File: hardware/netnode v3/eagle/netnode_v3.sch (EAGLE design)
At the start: 29 parts, among them IC1 TSR-1, IC2 PIC18F4K80, IC3 FOD060L, X1 DC10R, X2 XPORT

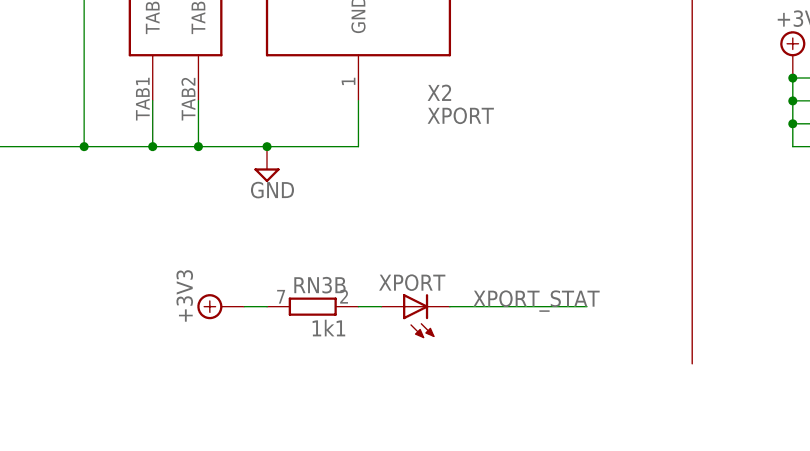
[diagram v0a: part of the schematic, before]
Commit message: Further board cleanup
* Silkscreen fixes + size increased
* Replaced 0603 componentsn with 0805 counterparts for easier soldering
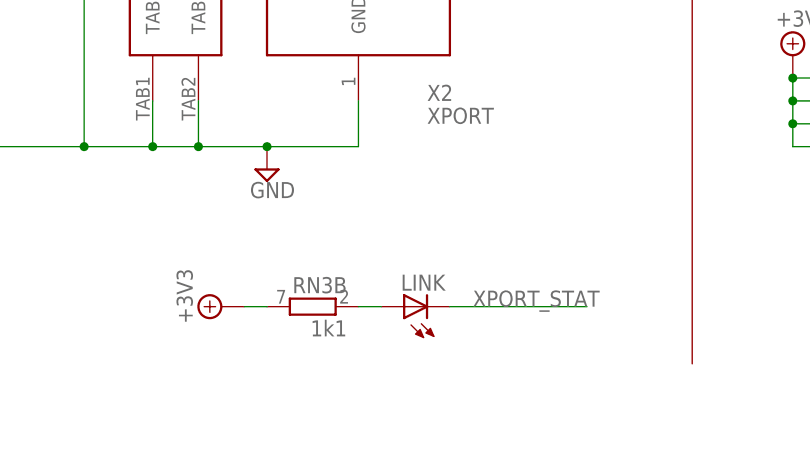
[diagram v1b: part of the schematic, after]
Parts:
- C1, C7: device netnode:C-EUC0603 -> rcl:C-EUC0805
- C3, C4: device rcl:C-EUC0603 -> rcl:C-EUC0805
- R1, R7: device rcl:R-EU_R0603 -> rcl:R-EU_R0805
- renumbered XPORT to LINK
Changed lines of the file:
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@@
 <attribute name="OC_FARNELL" value="8530025"/>
 </part>
-<part name="XPORT" library="led" deviceset="LED" device="CHIPLED_1206">
+<part name="LINK" library="led" deviceset="LED" device="CHIPLED_1206">
 <attribute name="MF" value="KINGBRIGHT"/>
 <attribute name="MPN" value="KP-3216EC"/>
@@
 <part name="V3" library="netnode" deviceset="+3V3" device=""/>
 <part name="V4" library="netnode" deviceset="+3V3" device=""/>
-<part name="C1" library="netnode" deviceset="C-EU" device="C0603" value="100n">
+<part name="C1" library="rcl" deviceset="C-EU" device="C0805" value="100n">
 <attribute name="MF" value="AVX"/>
 <attribute name="MPN" value="08055C104JAT2A"/>
@@
 <attribute name="OC_FARNELL" value="1823169"/>
 </part>
-<part name="R7" library="rcl" deviceset="R-EU_" device="R0603" value="2K">
+<part name="R7" library="rcl" deviceset="R-EU_" device="R0805" value="2K">
 <attribute name="MF" value="BOURNS"/>
 <attribute name="MPN" value="CR0603-FX-2001ELF"/>
@@
 </part>
 <part name="V11" library="netnode" deviceset="+3V3" device=""/>
-<part name="C3" library="rcl" deviceset="C-EU" device="C0603" value="100n">
+<part name="C3" library="rcl" deviceset="C-EU" device="C0805" value="100n">
 <attribute name="MF" value="AVX"/>
 <attribute name="MPN" value="08055C104JAT2A"/>
 <attribute name="OC_FARNELL" value="1740673"/>
 </part>
-<part name="C4" library="rcl" deviceset="C-EU" device="C0603" value="100n">
+<part name="C4" library="rcl" deviceset="C-EU" device="C0805" value="100n">
 <attribute name="MF" value="AVX"/>
 <attribute name="MPN" value="08055C104JAT2A"/>
@@
 </part>
 <part name="V26" library="supply2" deviceset="GND" device=""/>
-<part name="C7" library="netnode" deviceset="C-EU" device="C0603" value="100n">
+<part name="C7" library="rcl" deviceset="C-EU" device="C0805" value="100n">
 <attribute name="MF" value="AVX"/>
 <attribute name="MPN" value="08055C104JAT2A"/>
@@
 <part name="V34" library="netnode" deviceset="+3V3" device=""/>
 <part name="V35" library="netnode" deviceset="+3V3" device=""/>
-<part name="R1" library="rcl" deviceset="R-EU_" device="R0603" value="2K">
+<part name="R1" library="rcl" deviceset="R-EU_" device="R0805" value="2K">
 <attribute name="MF" value="BOURNS"/>
 <attribute name="MPN" value="CR0603-FX-2001ELF"/>
@@
 <attribute name="MPN" x="55.88" y="101.6" size="1.778" layer="96" rot="R90" display="off"/>
 </instance>
-<instance part="XPORT" gate="G$1" x="55.88" y="10.16" rot="R90">
+<instance part="LINK" gate="G$1" x="55.88" y="10.16" rot="R90">
 <attribute name="OC_FARNELL" x="55.88" y="10.16" size="1.778" layer="96" rot="R90" display="off"/>
 <attribute name="MF" x="55.88" y="10.16" size="1.778" layer="96" rot="R90" display="off"/>
@@
 </segment>
 <segment>
-<pinref part="XPORT" gate="G$1" pin="C"/>
+<pinref part="LINK" gate="G$1" pin="C"/>
 <wire x1="60.96" y1="10.16" x2="76.2" y2="10.16" width="0.1524" layer="91"/>
 <label x="63.5" y="10.16" size="1.778" layer="95"/>
@@
 <net name="N$1" class="1">
 <segment>
-<pinref part="XPORT" gate="G$1" pin="A"/>
+<pinref part="LINK" gate="G$1" pin="A"/>
 <wire x1="50.8" y1="10.16" x2="53.34" y2="10.16" width="0.1524" layer="91"/>
 <pinref part="RN3" gate="B" pin="1"/>

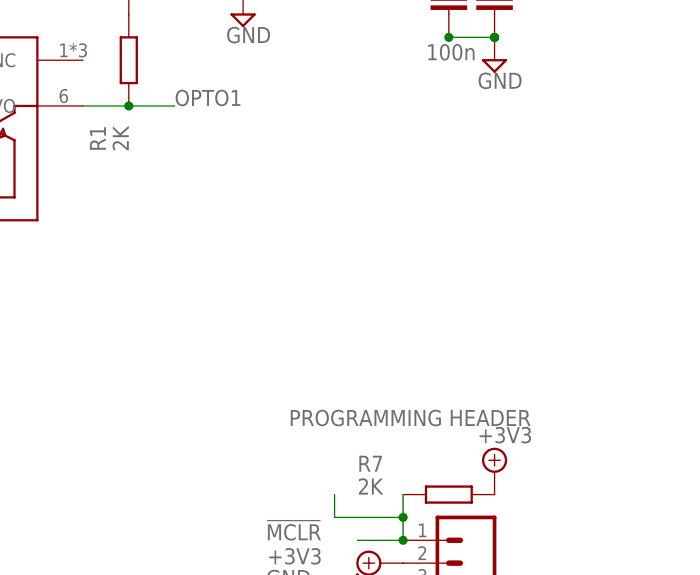
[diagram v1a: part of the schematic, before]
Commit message: Added reset button.
The reset button from Wuerth is a handy addition when developing firmware.
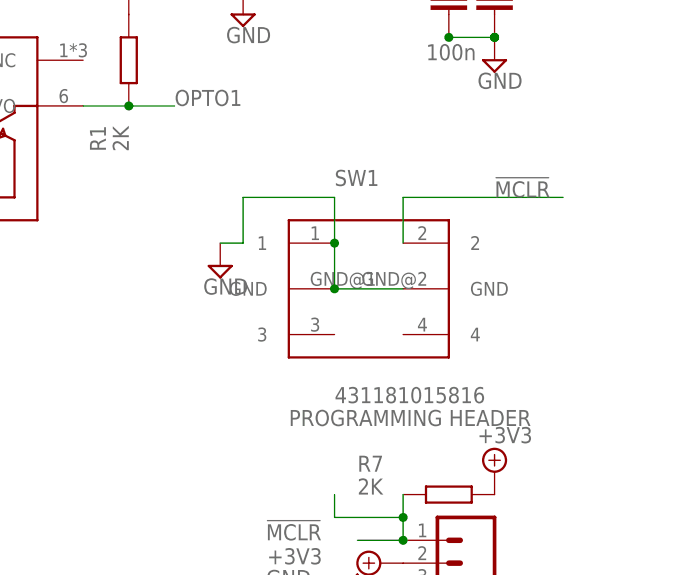
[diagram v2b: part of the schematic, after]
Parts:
- added SW1: 431181015816, Eagle_Wuerth_Elektronik_Switch_Power_Elements:431181015816
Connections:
- net !MCLR: now also SW1.2
- net GND: now also SW1.1, SW1.GND@1, SW1.GND@2
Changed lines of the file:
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@@
 <?xml version="1.0" encoding="utf-8"?>
 <!DOCTYPE eagle SYSTEM "eagle.dtd">
-<eagle version="6.2">
+<eagle version="6.3">
 <drawing>
 <settings>
@@
 <part name="R4" library="rcl" deviceset="R-EU_" device="R0603"/>
 <part name="R5" library="rcl" deviceset="R-EU_" device="R0603"/>
+<part name="SW1" library="Eagle_Wuerth_Elektronik_Switch_Power_Elements" deviceset="431181015816" device=""/>
+<part name="V6" library="supply2" deviceset="GND" device=""/>
 </parts>
 <sheets>
@@
 <instance part="R4" gate="G$1" x="114.3" y="66.04" rot="R90"/>
 <instance part="R5" gate="G$1" x="111.76" y="66.04" rot="R90"/>
+<instance part="SW1" gate="G$1" x="226.06" y="66.04"/>
+<instance part="V6" gate="GND" x="213.36" y="71.12"/>
 </instances>
 <busses>
@@
 <wire x1="124.46" y1="60.96" x2="132.08" y2="60.96" width="0.1524" layer="91"/>
 </segment>
+<segment>
+<wire x1="215.9" y1="78.74" x2="215.9" y2="73.66" width="0.1524" layer="91"/>
+<pinref part="V6" gate="GND" pin="GND"/>
+<wire x1="213.36" y1="73.66" x2="215.9" y2="73.66" width="0.1524" layer="91"/>
+<pinref part="SW1" gate="G$1" pin="1"/>
+<wire x1="226.06" y1="73.66" x2="226.06" y2="78.74" width="0.1524" layer="91"/>
+<wire x1="226.06" y1="78.74" x2="215.9" y2="78.74" width="0.1524" layer="91"/>
+<pinref part="SW1" gate="G$1" pin="GND@1"/>
+<wire x1="226.06" y1="68.58" x2="226.06" y2="73.66" width="0.1524" layer="91"/>
+<junction x="226.06" y="73.66"/>
+<pinref part="SW1" gate="G$1" pin="GND@2"/>
+<wire x1="226.06" y1="68.58" x2="233.68" y2="68.58" width="0.1524" layer="91"/>
+<junction x="226.06" y="68.58"/>
+</segment>
 </net>
 <net name="VSUPPLY" class="1">
@@
 <label x="129.54" y="121.92" size="1.778" layer="95"/>
 </segment>
-</net>
+<segment>
+<wire x1="233.68" y1="78.74" x2="251.46" y2="78.74" width="0.1524" layer="91"/>
+<label x="243.84" y="78.74" size="1.778" layer="95"/>
+<pinref part="SW1" gate="G$1" pin="2"/>
+<wire x1="233.68" y1="73.66" x2="233.68" y2="78.74" width="0.1524" layer="91"/>
+</segment>
+</net>
